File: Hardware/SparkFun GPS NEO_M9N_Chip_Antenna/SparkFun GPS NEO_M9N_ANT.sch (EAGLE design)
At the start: 51 parts, among them J2 Qwiic Right Angle, J4 Qwiic Right Angle, U1 U-BLOX_NEO-M9N, U2 3.3V, Y1 GPS_CHIP_ANTENNAW3011

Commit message: Updates both designs with 5.1k resistor in 0603 package
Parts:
- R12, R13: device SparkFun-Resistors:5.1KOHM-0402-1/16W-1% -> SparkFun-Resistors:5.1KOHM5.1KOHM-0603-1/10W-1%
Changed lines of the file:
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@@
 <part name="J5" library="SparkFun-Connectors" deviceset="CONN_04" device="1X04_NO_SILK"/>
 <part name="J3" library="SparkFun-Connectors" deviceset="USB_C" device="2-LAYER"/>
-<part name="R12" library="SparkFun-Resistors" deviceset="5.1KOHM" device="-0402-1/16W-1%" value="5.1k"/>
-<part name="R13" library="SparkFun-Resistors" deviceset="5.1KOHM" device="-0402-1/16W-1%" value="5.1k"/>
+<part name="R12" library="SparkFun-Resistors" deviceset="5.1KOHM" device="5.1KOHM-0603-1/10W-1%" value="5.1k"/>
+<part name="R13" library="SparkFun-Resistors" deviceset="5.1KOHM" device="5.1KOHM-0603-1/10W-1%" value="5.1k"/>
 <part name="GND9" library="SparkFun-PowerSymbols" deviceset="GND" device=""/>
 <part name="GND17" library="SparkFun-PowerSymbols" deviceset="GND" device=""/>

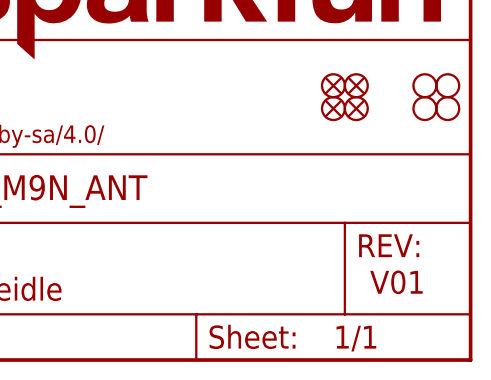
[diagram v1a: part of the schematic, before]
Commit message: Changes version to v02
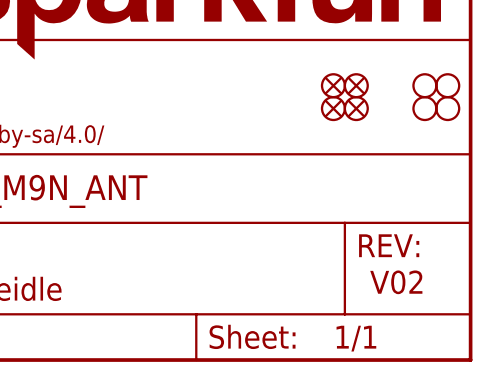
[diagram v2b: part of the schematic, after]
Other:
- note added: "V02"
- note removed: "V01"
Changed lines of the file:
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@@
 <?xml version="1.0" encoding="utf-8"?>
 <!DOCTYPE eagle SYSTEM "eagle.dtd">
-<eagle version="9.4.2">
+<eagle version="9.5.1">
 <drawing>
 <settings>
@@
 <sheet>
 <plain>
-<text x="237.744" y="7.366" size="2.54" layer="94" font="vector">V01</text>
+<text x="237.744" y="7.366" size="2.54" layer="94" font="vector">V02</text>
 <text x="55.88" y="119.38" size="1.778" layer="97" font="vector" align="center">7-bit unshifted I2C address: 0x42</text>
 <wire x1="0" y1="106.68" x2="73.66" y2="106.68" width="0.1524" layer="97" style="shortdash"/>

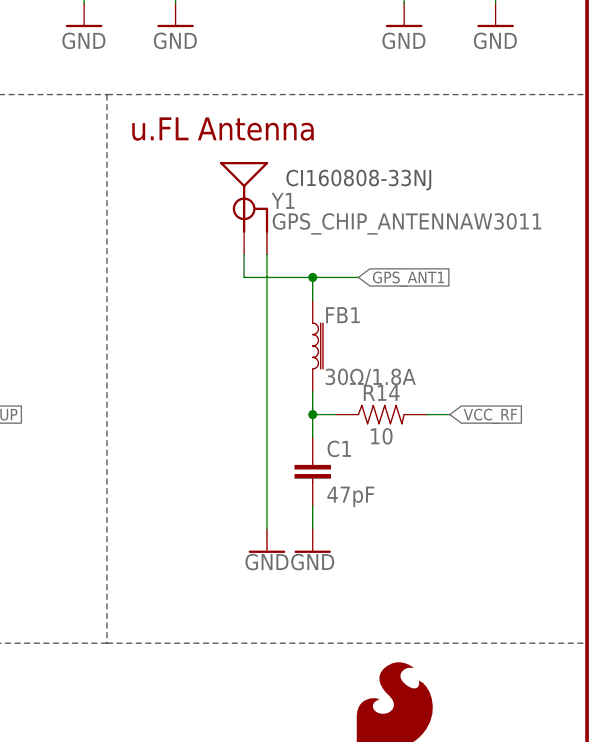
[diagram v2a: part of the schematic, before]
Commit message: Removes VCC bias to antenna from antenna design
* Deletes all gerber files related to prototypes
* Moves GPS library out of the buzzard label folder
* Deletes buzzard labels
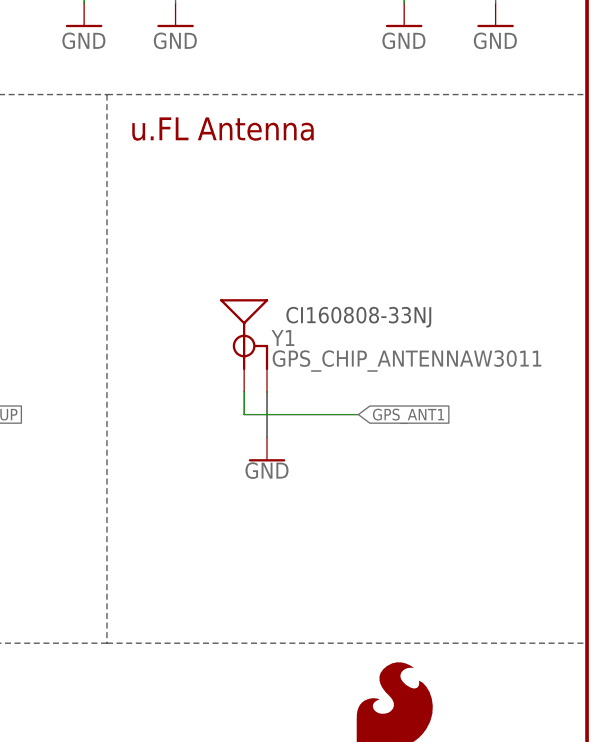
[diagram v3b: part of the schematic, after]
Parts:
- removed C1: 47pF, SparkFun-Capacitors:47PF-0603-50V-5%
- removed FB1: 30Ω/1.8A, SparkFun-Coils:FERRITE_BEAD-0603
- removed R14: 10, SparkFun-Resistors:10OHM-0603-1/10W-1%
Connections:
- removed net ANT_VCC: C1.1, FB1.2, R14.1
- net GND: no longer C1.2
- net GPS_ANT1: no longer FB1.1
- net VCC_RF: no longer R14.2
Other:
- moved on the sheet: Y1
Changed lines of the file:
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@@
 <part name="R7" library="SparkFun-Resistors" deviceset="2.2KOHM" device="-0603-1/10W-1%" value="2.2k"/>
 <part name="R8" library="SparkFun-Resistors" deviceset="2.2KOHM" device="-0603-1/10W-1%" value="2.2k"/>
-<part name="JP5" library="SparkFun-Jumpers" deviceset="JUMPER-SMT_3_2-NC_TRACE" device="_SILK" value="JUMPER-SMT_3_2-NC_TRACE_SILK"/>
+<part name="JP5" library="SparkFun-Jumpers" deviceset="JUMPER-SMT_3_2-NC_TRACE" device="_SILK" package3d_urn="urn:adsk.eagle:package:39289/1" value="JUMPER-SMT_3_2-NC_TRACE_SILK"/>
 <part name="SUPPLY9" library="SparkFun-PowerSymbols" deviceset="3.3V" device=""/>
 <part name="GND4" library="SparkFun-PowerSymbols" deviceset="GND" device=""/>
 <part name="LED1" library="SparkFun-LED" deviceset="LED-BLUE" device="0603" value="BLUE"/>
-<part name="PPS" library="SparkFun-Jumpers" deviceset="JUMPER-SMT_2_NC_TRACE" device="_SILK" value="JUMPER-SMT_2_NC_TRACE_SILK"/>
+<part name="PPS" library="SparkFun-Jumpers" deviceset="JUMPER-SMT_2_NC_TRACE" device="_SILK" package3d_urn="urn:adsk.eagle:package:39281/1" value="JUMPER-SMT_2_NC_TRACE_SILK"/>
 <part name="D2" library="SparkFun-DiscreteSemi" deviceset="DIODE-SCHOTTKY" device="-PMEG4005EJ" value="0.5A/40V/420mV"/>
 <part name="SUPPLY5" library="SparkFun-PowerSymbols" deviceset="3.3V" device=""/>
@@
 <part name="R9" library="SparkFun-Resistors" deviceset="27OHM" device="-0603-1/10W-1%" value="27"/>
 <part name="R10" library="SparkFun-Resistors" deviceset="27OHM" device="-0603-1/10W-1%" value="27"/>
-<part name="SPI" library="SparkFun-Jumpers" deviceset="JUMPER-SMT_2_NO" device="_SILK" value="JUMPER-SMT_2_NO_SILK"/>
+<part name="SPI" library="SparkFun-Jumpers" deviceset="JUMPER-SMT_2_NO" device="_SILK" package3d_urn="urn:adsk.eagle:package:39279/1" value="JUMPER-SMT_2_NO_SILK"/>
 <part name="GND2" library="SparkFun-PowerSymbols" deviceset="GND" device=""/>
-<part name="C1" library="SparkFun-Capacitors" deviceset="47PF" device="-0603-50V-5%" value="47pF"/>
-<part name="R14" library="SparkFun-Resistors" deviceset="10OHM" device="-0603-1/10W-1%" value="10"/>
-<part name="GND18" library="SparkFun-PowerSymbols" deviceset="GND" device=""/>
 <part name="R15" library="SparkFun-Resistors" deviceset="100KOHM" device="-0603-1/10W-1%" value="100k"/>
 <part name="SUPPLY6" library="SparkFun-PowerSymbols" deviceset="3.3V" device=""/>
-<part name="FB1" library="SparkFun-Coils" deviceset="FERRITE_BEAD" device="-0603" value="30Ω/1.8A"/>
 <part name="JP15" library="SparkFun-Connectors" deviceset="CONN_04" device="1X04_NO_SILK"/>
 <part name="SUPPLY10" library="SparkFun-PowerSymbols" deviceset="3.3V" device=""/>
@@
 <part name="LOGO2" library="SparkFun-Aesthetics" deviceset="SFE_LOGO_NAME_FLAME" device=".1_INCH"/>
 <part name="U1" library="gps" deviceset="U-BLOX_NEO-M9N" device=""/>
-<part name="PWR\" library="SparkFun-Jumpers" deviceset="JUMPER-SMT_2_NC_TRACE" device="_SILK" value="JUMPER-SMT_2_NC_TRACE_SILK"/>
+<part name="PWR\" library="SparkFun-Jumpers" deviceset="JUMPER-SMT_2_NC_TRACE" device="_SILK" package3d_urn="urn:adsk.eagle:package:39281/1" value="JUMPER-SMT_2_NC_TRACE_SILK"/>
 <part name="D3" library="SparkFun-IC-Power" deviceset="PRTR5V0U2" device="F"/>
 <part name="J5" library="SparkFun-Connectors" deviceset="CONN_04" device="1X04_NO_SILK"/>
@@
 <text x="43.18" y="12.7" size="1.778" layer="97" font="vector">Close jumper to
 enable SPI</text>
-<text x="215.392" y="111.76" size="1.778" layer="97" font="vector">CI160808-33NJ</text>
+<text x="215.392" y="96.52" size="1.778" layer="97" font="vector">CI160808-33NJ</text>
 <text x="166.624" y="11.176" size="2.54" layer="94" font="vector">Elias Santistevan</text>
 <text x="78.74" y="99.06" size="2.54" layer="94" font="vector">Headers</text>
@@
 <attribute name="VALUE" x="129.54" y="127" size="1.778" layer="96" font="vector"/>
 </instance>
-<instance part="GND27" gate="1" x="213.36" y="71.12" smashed="yes">
-<attribute name="VALUE" x="213.36" y="70.866" size="1.778" layer="96" font="vector" align="top-center"/>
+<instance part="GND27" gate="1" x="213.36" y="81.28" smashed="yes">
+<attribute name="VALUE" x="213.36" y="81.026" size="1.778" layer="96" font="vector" align="top-center"/>
 </instance>
 <instance part="C4" gate="G$1" x="228.6" y="154.94" smashed="yes">
@@
 <attribute name="VALUE" x="40.64" y="7.366" size="1.778" layer="96" font="vector" align="top-center"/>
 </instance>
-<instance part="C1" gate="G$1" x="218.44" y="78.74" smashed="yes">
-<attribute name="NAME" x="219.964" y="81.661" size="1.778" layer="95" font="vector"/>
-<attribute name="VALUE" x="219.964" y="76.581" size="1.778" layer="96" font="vector"/>
-</instance>
-<instance part="R14" gate="G$1" x="226.06" y="86.36" smashed="yes">
-<attribute name="NAME" x="226.06" y="87.884" size="1.778" layer="95" font="vector" align="bottom-center"/>
-<attribute name="VALUE" x="226.06" y="84.836" size="1.778" layer="96" font="vector" align="top-center"/>
-</instance>
-<instance part="GND18" gate="1" x="218.44" y="71.12" smashed="yes">
-<attribute name="VALUE" x="218.44" y="70.866" size="1.778" layer="96" font="vector" align="top-center"/>
-</instance>
 <instance part="R15" gate="G$1" x="22.86" y="127" smashed="yes" rot="R90">
 <attribute name="NAME" x="21.336" y="127" size="1.778" layer="95" font="vector" rot="R90" align="bottom-center"/>
@@
 <instance part="SUPPLY6" gate="G$1" x="22.86" y="165.1" smashed="yes" rot="MR0">
 <attribute name="VALUE" x="22.86" y="167.894" size="1.778" layer="96" font="vector" rot="MR0" align="bottom-center"/>
-</instance>
-<instance part="FB1" gate="G$1" x="218.44" y="93.98" smashed="yes">
-<attribute name="NAME" x="219.71" y="96.52" size="1.778" layer="95" font="vector"/>
-<attribute name="VALUE" x="219.71" y="91.44" size="1.778" layer="96" font="vector" align="top-left"/>
 </instance>
 <instance part="JP15" gate="J1" x="101.6" y="88.9" smashed="yes" rot="MR0">
@@
 <attribute name="VALUE" x="40.64" y="43.434" size="1.778" layer="96" font="vector" align="bottom-center"/>
 </instance>
-<instance part="Y1" gate="G$1" x="210.82" y="114.3" smashed="yes">
-<attribute name="NAME" x="213.868" y="109.22" size="1.778" layer="95" font="vector"/>
-<attribute name="VALUE" x="213.868" y="106.934" size="1.778" layer="96" font="vector"/>
+<instance part="Y1" gate="G$1" x="210.82" y="99.06" smashed="yes">
+<attribute name="NAME" x="213.868" y="93.98" size="1.778" layer="95" font="vector"/>
+<attribute name="VALUE" x="213.868" y="91.694" size="1.778" layer="96" font="vector"/>
 </instance>
 </instances>
@@
 </segment>
 <segment>
-<pinref part="C1" gate="G$1" pin="2"/>
-<pinref part="GND18" gate="1" pin="GND"/>
-<wire x1="218.44" y1="73.66" x2="218.44" y2="76.2" width="0.1524" layer="91"/>
-</segment>
-<segment>
 <pinref part="J1" gate="J1" pin="1"/>
 <pinref part="GND1" gate="1" pin="GND"/>
@@
 <segment>
 <pinref part="Y1" gate="G$1" pin="GND"/>
-<wire x1="213.36" y1="104.14" x2="213.36" y2="73.66" width="0.1524" layer="91"/>
+<wire x1="213.36" y1="88.9" x2="213.36" y2="83.82" width="0.1524" layer="91"/>
 <pinref part="GND27" gate="1" pin="GND"/>
 </segment>
@@
 <net name="GPS_ANT1" class="3">
 <segment>
-<wire x1="218.44" y1="101.6" x2="218.44" y2="99.06" width="0.1524" layer="91"/>
-<pinref part="FB1" gate="G$1" pin="1"/>
-<wire x1="223.52" y1="101.6" x2="218.44" y2="101.6" width="0.1524" layer="91"/>
-<junction x="218.44" y="101.6"/>
-<label x="223.52" y="101.6" size="1.27" layer="95" xref="yes"/>
-<wire x1="210.82" y1="101.6" x2="218.44" y2="101.6" width="0.1524" layer="91"/>
-<wire x1="210.82" y1="101.6" x2="210.82" y2="104.14" width="0.1524" layer="91"/>
+<label x="223.52" y="86.36" size="1.27" layer="95" xref="yes"/>
+<wire x1="210.82" y1="86.36" x2="223.52" y2="86.36" width="0.1524" layer="91"/>
+<wire x1="210.82" y1="86.36" x2="210.82" y2="88.9" width="0.1524" layer="91"/>
 <pinref part="Y1" gate="G$1" pin="SIGNAL"/>
 </segment>
@@
 <label x="20.32" y="149.86" size="1.27" layer="95" rot="R180" xref="yes"/>
 </segment>
-<segment>
-<pinref part="R14" gate="G$1" pin="2"/>
-<wire x1="233.68" y1="86.36" x2="231.14" y2="86.36" width="0.1524" layer="91"/>
-<label x="233.68" y="86.36" size="1.27" layer="95" xref="yes"/>
-</segment>
-</net>
-<net name="ANT_VCC" class="0">
-<segment>
-<pinref part="R14" gate="G$1" pin="1"/>
-<wire x1="220.98" y1="86.36" x2="218.44" y2="86.36" width="0.1524" layer="91"/>
-<pinref part="C1" gate="G$1" pin="1"/>
-<wire x1="218.44" y1="86.36" x2="218.44" y2="83.82" width="0.1524" layer="91"/>
-<wire x1="218.44" y1="88.9" x2="218.44" y2="86.36" width="0.1524" layer="91"/>
-<junction x="218.44" y="86.36"/>
-<pinref part="FB1" gate="G$1" pin="2"/>
-</segment>
 </net>
 <net name="D+" class="0">
@@
 which will not be processed correctly with this version.
 </note>
+<note version="8.3" severity="warning">
+Since Version 8.3, EAGLE supports URNs for individual library
+assets (packages, symbols, and devices). The URNs of those assets
+will not be understood (or retained) with this version.
+</note>
+<note version="8.3" severity="warning">
+Since Version 8.3, EAGLE supports the association of 3D packages
+with devices in libraries, schematics, and board files. Those 3D
+packages will not be understood (or retained) with this version.
+</note>
 </compatibility>

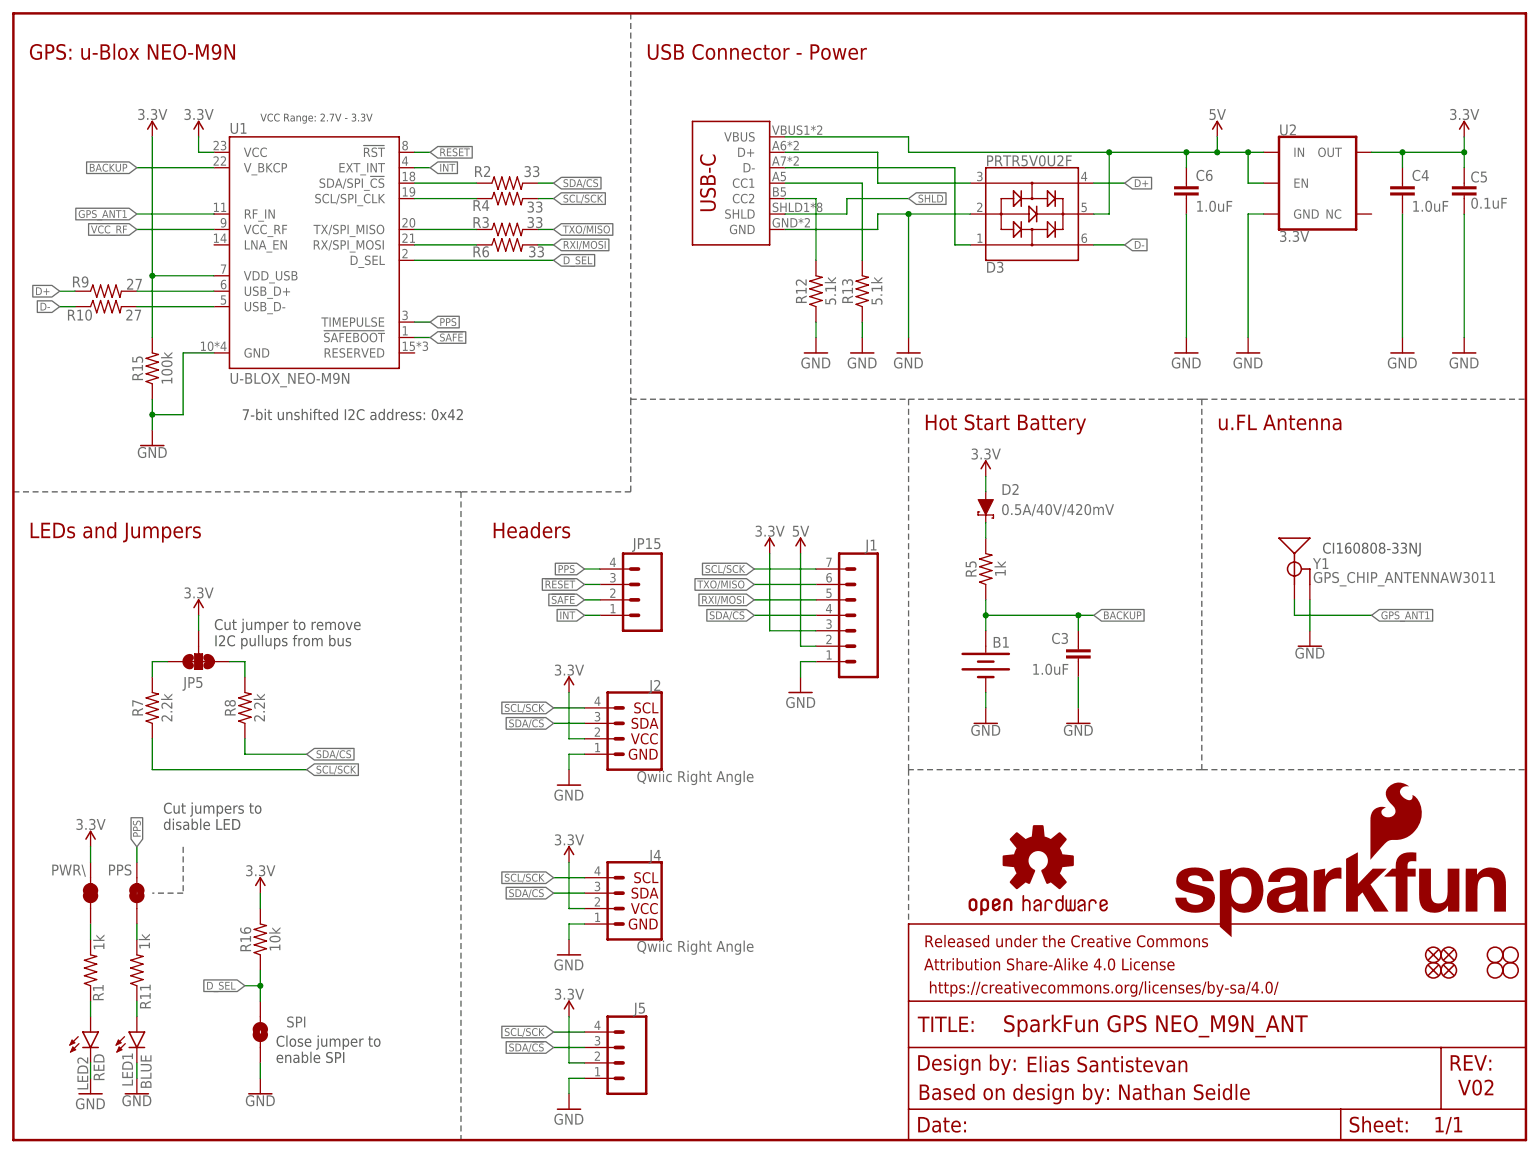
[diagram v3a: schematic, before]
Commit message: Updates Schematic to be more neat
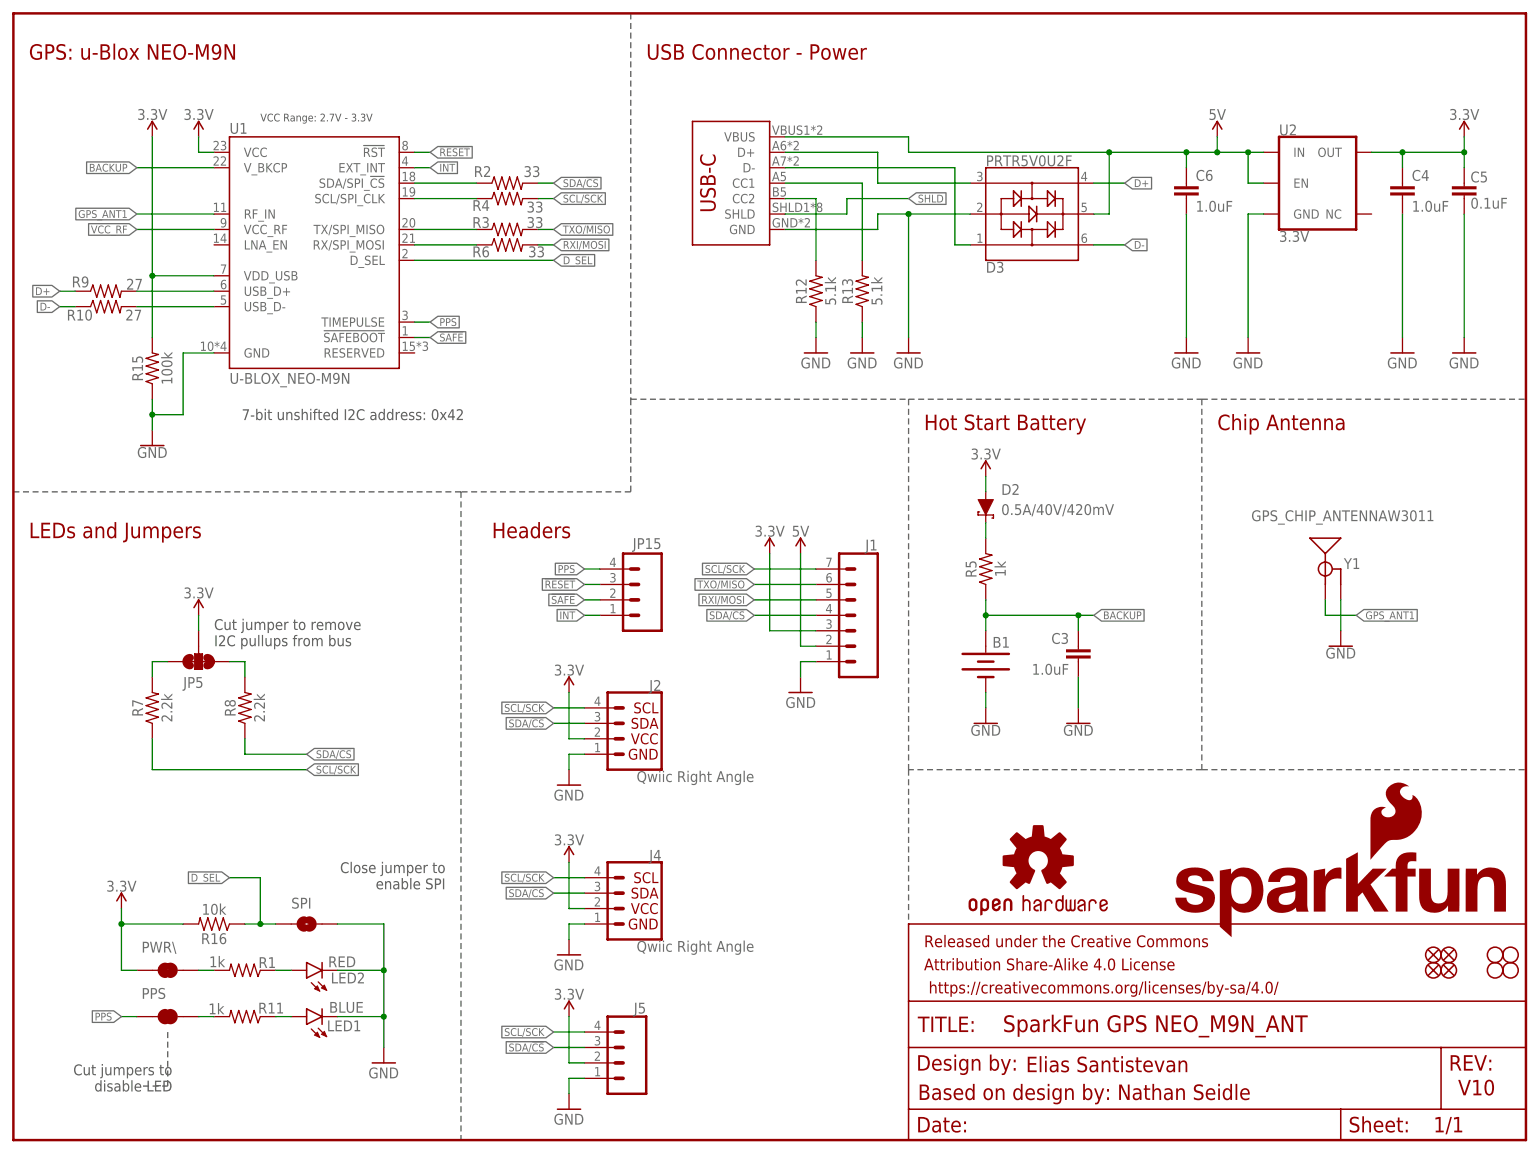
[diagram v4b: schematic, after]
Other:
- note added: "Chip Antenna"
- note added: "V10"
- note removed: "CI160808-33NJ"
- note removed: "V02"
- note removed: "u.FL Antenna"
- moved on the sheet: LED1, LED2, PPS, PWR\, R1, R11, R16, SPI, Y1
